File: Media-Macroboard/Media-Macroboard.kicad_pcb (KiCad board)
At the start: 2 copper layers, 100 x 100 mm, 84 parts, among them IC1 MCP73871-4CCI_ML, IC2 LM1117MPX-33NOPB, J1 SS-52400-002, J2 B2B-PH-SM4-TB_LF__SN_, J3 Conn_01x04_MountingPin, Q1 MMBT3904LT3G, Q2 MMBT3904LT3G, Q4 TEMT6000X01, SW1 SW_MEC_5G, SW12 SW_MEC_5G, SW2 SW_MEC_5G, SW3 SW_MEC_5G, SW4 SW_MEC_5G, SW5 SW_MEC_5G, SW6 SW_MEC_5G, SW7 SW_MEC_5G, SW8 SW_MEC_5G, SW9 SW_MEC_5G, U1 ESP32-S3-WROOM-1, U2 USBLC6-2SC6, U3 CP2102N-Axx-xQFN20

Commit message: First productable version
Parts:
- added R23: 470, Resistor_SMD:R_0805_2012Metric_Pad1.20x1.40mm_HandSolder, B.Cu at (100.5, 149.5)
- added R24: 470, Resistor_SMD:R_0805_2012Metric_Pad1.20x1.40mm_HandSolder, B.Cu at (190.0, 151.0)
- added R25: 470, Resistor_SMD:R_0805_2012Metric_Pad1.20x1.40mm_HandSolder, B.Cu at (192.0, 104.0)
- C4, C6, C9: footprint Capacitor_SMD:C_0805_2012Metric_Pad1.18x1.45mm_HandSolder -> Capacitor_SMD:C_1206_3216Metric
- moved U3 13.0 mm to (154.8, 65.0), turned to 90 degrees
- moved LED6 10.8 mm to (155.8, 80.2)
- moved R15 10.8 mm to (155.8, 76.2), turned to -90 degrees
- moved U2 9.95 mm to (164.5, 75.8)
- moved C8 9.55 mm to (176.9, 56.0), turned to 0 degrees
- moved R11 9.00 mm to (159.6, 69.0), turned to 180 degrees
- moved LED2 8.63 mm to (174.9, 77.6)
- moved R9 8.63 mm to (174.9, 81.6)
- moved LED3 8.50 mm to (183.0, 77.5)
- moved R7 8.50 mm to (183.0, 81.4)
- moved Q4 8.36 mm to (168.9, 56.5)
- moved R16 8.02 mm to (159.6, 61.0), turned to 0 degrees
- moved LED5 6.72 mm to (158.2, 80.2)
- moved R14 6.72 mm to (158.2, 76.2), turned to -90 degrees
- moved R12 5.37 mm to (159.6, 67.0), turned to 0 degrees
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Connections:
- LED7 pad 1: Net-(LED10-K) -> Net-(LED7-K)
- LED8 pad 1: Net-(LED10-K) -> Net-(LED8-K)
- LED9 pad 1: Net-(LED10-K) -> Net-(LED9-K)
- R19 pad 1: Net-(LED10-K) -> Net-(LED7-K)
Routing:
- net /ESP32-S3-01/ROW_3: track 0.00 -> 135.2 mm, vias 0 -> 3
- net /ESP32-S3-01/LED3: track 0.00 -> 120.4 mm, vias 0 -> 1
- net /ESP32-S3-01/ROW_2: track 0.00 -> 115.7 mm, vias 0 -> 3
- net /ESP32-S3-01/LED2: track 0.00 -> 107.8 mm, vias 0 -> 1
- net GND: track 0.00 -> 107.2 mm, vias 0 -> 27
- net /ESP32-S3-01/ROW_1: track 0.00 -> 95.9 mm, vias 0 -> 1
- net /ESP32-S3-01/JoyStick_1: track 0.00 -> 95.1 mm, vias 0 -> 2
- net /ESP32-S3-01/JoyStick_Button: track 0.00 -> 92.1 mm, vias 0 -> 2
- net /ESP32-S3-01/JoyStick_2: track 0.00 -> 87.7 mm, vias 0 -> 2
- net /ESP32-S3-01/COL_4: track 0.00 -> 87.0 mm
- net /ESP32-S3-01/COL_1: track 0.00 -> 80.5 mm, vias 0 -> 2
- net /VBUS: track 0.00 -> 77.5 mm, vias 0 -> 2
- net /ESP32-S3-01/LED4: track 0.00 -> 71.1 mm, vias 0 -> 1
- net /ESP32-S3-01/GPIO0: track 0.00 -> 62.4 mm, vias 0 -> 2
- net /ESP32-S3-01/DTR: track 0.00 -> 57.3 mm, vias 0 -> 2
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- added copper zone on F.Cu, net +3.3V

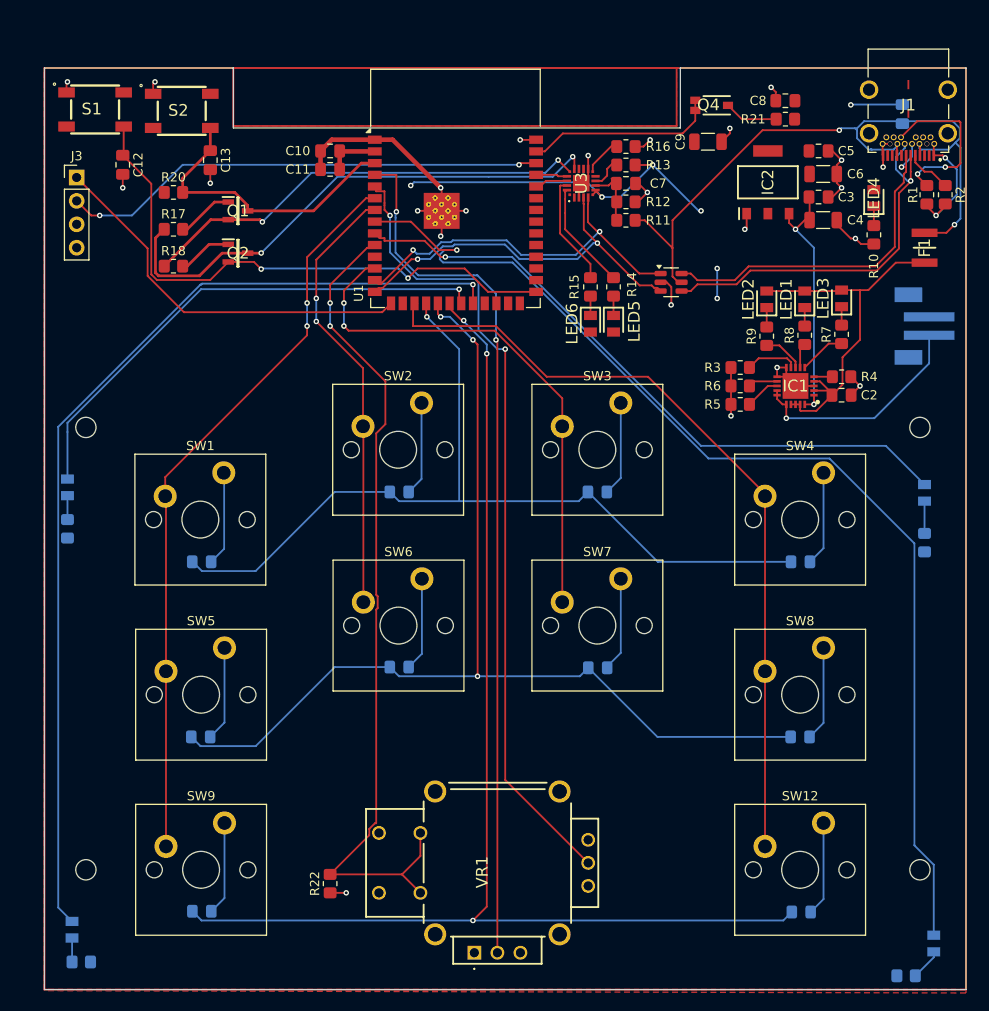
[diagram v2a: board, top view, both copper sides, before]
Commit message: Made four-layer version
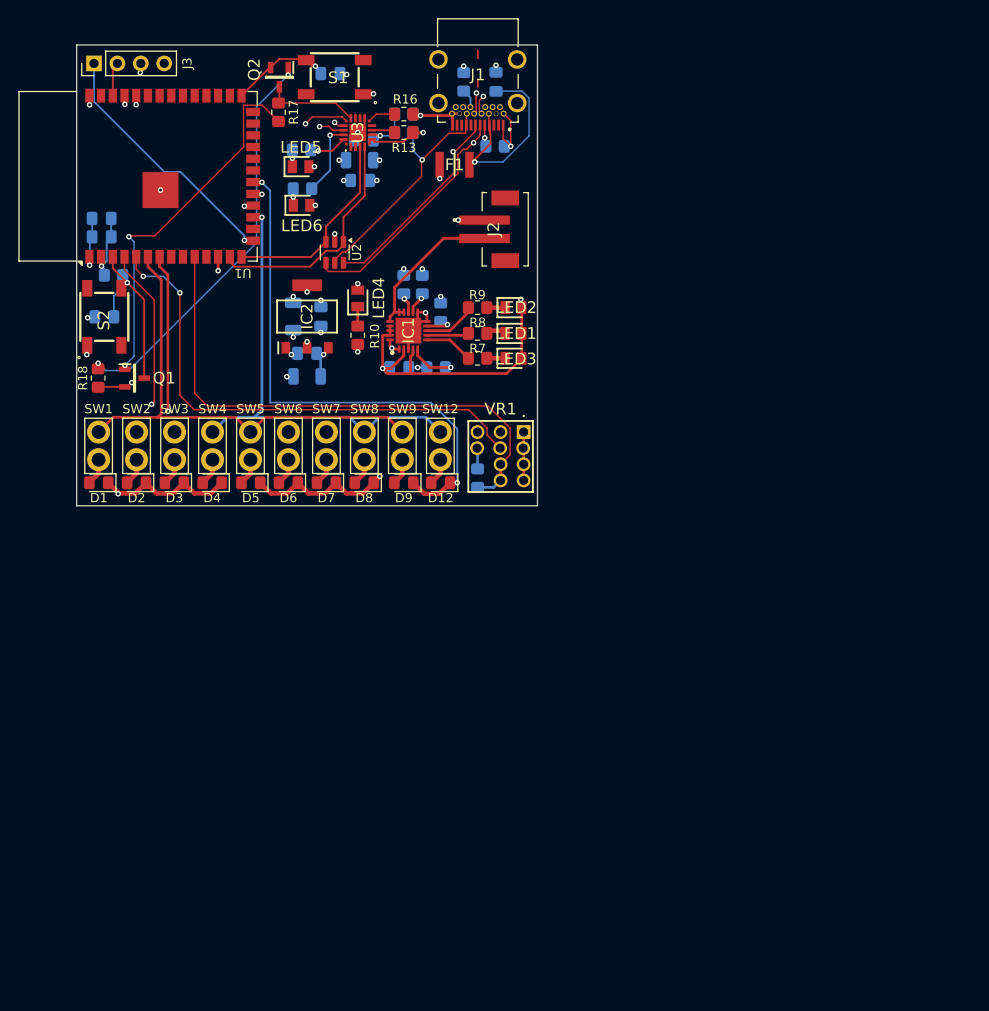
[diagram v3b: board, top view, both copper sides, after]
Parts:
- removed LED10, LED7, LED8, LED9: LTST-C170TBKT, Footprints:LEDC2012X120N
- removed Q4: TEMT6000X01, Footprints:TEMT6000X01
- removed R19, R23, R24, R25: 470, Resistor_SMD:R_0805_2012Metric_Pad1.20x1.40mm_HandSolder
- removed R21: 10K, Resistor_SMD:R_0805_2012Metric_Pad1.20x1.40mm_HandSolder
- removed REF** (x4): MountingHole_2.2mm_M2_ISO14580, MountingHole:MountingHole_2.2mm_M2_ISO14580
- C10, C11, C12, C13, C2, C3, C4, C5, C6, C7, C8, C9, R1, R11, R12, R14, R15, R2, R20, R22, R3, R4, R5, R6: moved to B.Cu
- D1, D12, D2, D3, D4, D5, D6, D7, D8, D9, J2: moved to F.Cu
- SW1, SW12, SW2, SW3, SW4, SW5, SW6, SW7, SW8, SW9: footprint PCM_Switch_Keyboard_Cherry_MX:SW_Cherry_MX_PCB_1.00u -> PCM_Switch_Keyboard_Cherry_MX:SW_Cherry_Compact
- moved D4 64.4 mm to (114.7, 97.5), turned to 180 degrees
- moved SW4 64.3 mm to (114.7, 93.5)
- moved D12 60.8 mm to (139.5, 97.5), turned to 180 degrees
- moved SW12 60.3 mm to (139.5, 93.5)
- moved C6 59.5 mm to (123.5, 79.5), turned to -90 degrees
- moved C4 58.5 mm to (125.0, 86.0), turned to 180 degrees
- moved C3 58.0 mm to (125.0, 83.5), turned to 180 degrees
- moved LED4 57.1 mm to (130.5, 77.5)
- moved R10 57.1 mm to (130.5, 81.5)
- moved C5 56.9 mm to (126.5, 79.5), turned to -90 degrees
- moved VR1 56.8 mm to (148.5, 92.0), turned to -90 degrees
- moved D8 54.8 mm to (131.2, 97.5), turned to 180 degrees
- moved SW8 54.4 mm to (131.2, 93.5)
- moved IC2 52.1 mm to (125.0, 79.5)
- moved F1 51.8 mm to (141.0, 63.0), turned to 0 degrees
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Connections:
- U1 pad 21: /ESP32-S3-01/LED1 -> unconnected-(U1-IO13-Pad21)
- U1 pad 22: /ESP32-S3-01/LED2 -> unconnected-(U1-IO14-Pad22)
- U1 pad 39: /ESP32-S3-01/Light -> unconnected-(U1-IO1-Pad39)
- U1 pad 8: /ESP32-S3-01/LED3 -> unconnected-(U1-IO15-Pad8)
- U1 pad 9: /ESP32-S3-01/LED4 -> unconnected-(U1-IO16-Pad9)
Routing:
- net /ESP32-S3-01/LED3: track 120.4 -> 0.00 mm, vias 1 -> 0
- net /ESP32-S3-01/LED2: track 107.8 -> 0.00 mm, vias 1 -> 0
- net /ESP32-S3-01/ROW_3: track 135.2 -> 56.6 mm, vias 3 -> 2
- net GND: track 107.2 -> 33.1 mm, vias 27 -> 26
- net /ESP32-S3-01/LED4: track 71.1 -> 0.00 mm, vias 1 -> 0
- net /ESP32-S3-01/ROW_2: track 115.7 -> 57.8 mm, vias 3 -> 2
- net /ESP32-S3-01/LED1: track 56.2 -> 0.00 mm, vias 1 -> 0
- net /ESP32-S3-01/GPIO0: track 62.4 -> 9.98 mm, vias 2 -> 1
- net /ESP32-S3-01/SCL: track 52.9 -> 3.71 mm, vias 2 -> 0
- net /ESP32-S3-01/DTR: track 57.3 -> 10.3 mm, vias 2 -> 0
- net /ESP32-S3-01/ROW_1: track 95.9 -> 52.2 mm, vias 1 -> 2
- net /ESP32-S3-01/JoyStick_1: track 95.1 -> 56.5 mm, vias 2 -> 1
- net /ESP32-S3-01/COL_4: track 87.0 -> 49.4 mm, vias 0 -> 1
- net Net-(Q2-B): track 5.93 -> 42.9 mm, vias 0 -> 2
- net Net-(Q1-B): track 6.17 -> 40.1 mm, vias 0 -> 2
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- added copper zone on In1.Cu, net +3.3V
- added copper zone on In2.Cu, net GND
- removed copper zone on F.Cu, net +3.3V
- removed copper zone on B.Cu, net GND
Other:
- board size 100 x 100 mm -> 50 x 50 mm
- copper layers 2 -> 4

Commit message: Added more rows and columns
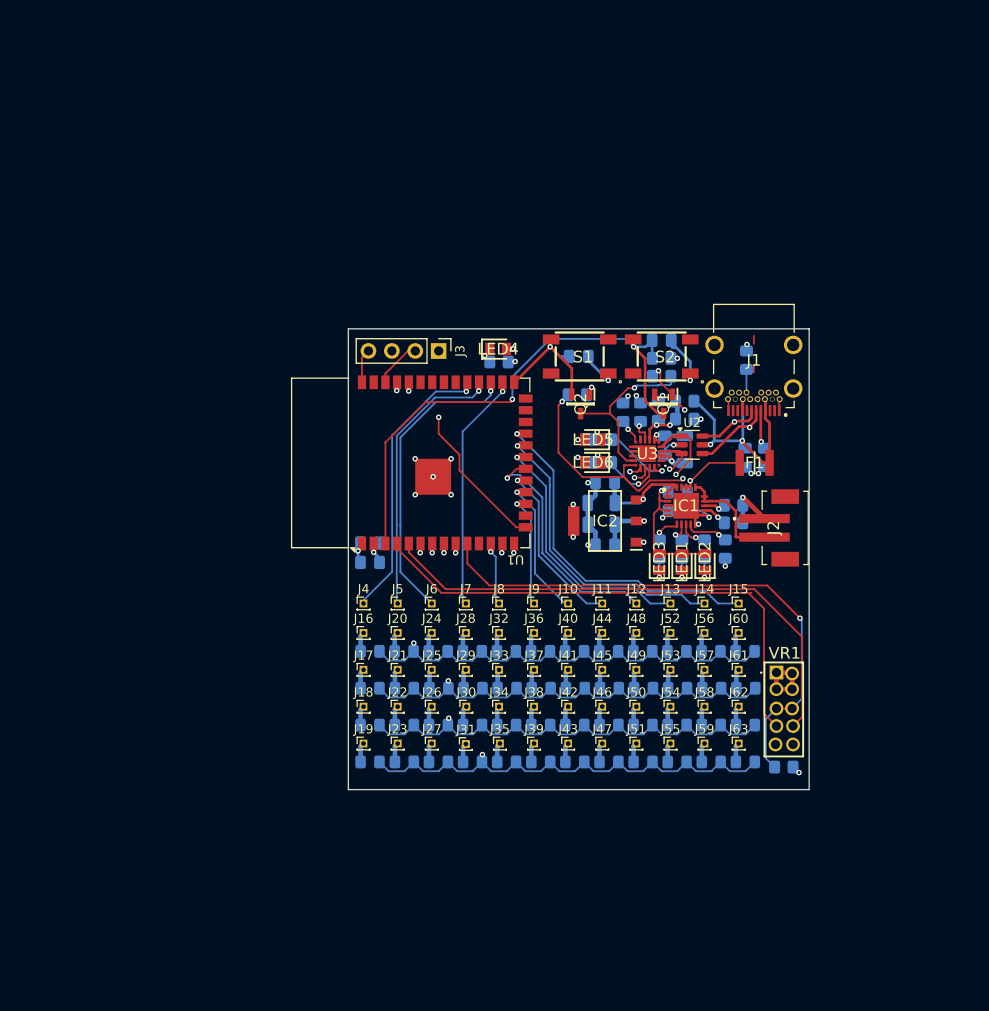
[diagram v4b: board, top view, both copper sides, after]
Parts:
- removed SW1, SW12, SW2, SW3, SW4, SW5, SW6, SW7, SW8, SW9: SW_MEC_5G, PCM_Switch_Keyboard_Cherry_MX:SW_Cherry_Compact
- added D10: D, Diode_SMD:D_0805_2012Metric_Pad1.15x1.40mm_HandSolder, B.Cu at (135.6, 123.8)
- added D11: D, Diode_SMD:D_0805_2012Metric_Pad1.15x1.40mm_HandSolder, B.Cu at (139.3, 123.8)
- added D13: D, Diode_SMD:D_0805_2012Metric_Pad1.15x1.40mm_HandSolder, B.Cu at (131.8, 127.8)
- added D14: D, Diode_SMD:D_0805_2012Metric_Pad1.15x1.40mm_HandSolder, B.Cu at (135.6, 127.8)
- added D15: D, Diode_SMD:D_0805_2012Metric_Pad1.15x1.40mm_HandSolder, B.Cu at (139.3, 127.8)
- added D16: D, Diode_SMD:D_0805_2012Metric_Pad1.15x1.40mm_HandSolder, B.Cu at (143.0, 127.8)
- added D17: D, Diode_SMD:D_0805_2012Metric_Pad1.15x1.40mm_HandSolder, B.Cu at (146.6, 115.8)
- added D18: D, Diode_SMD:D_0805_2012Metric_Pad1.15x1.40mm_HandSolder, B.Cu at (146.7, 119.8)
- added D19: D, Diode_SMD:D_0805_2012Metric_Pad1.15x1.40mm_HandSolder, B.Cu at (146.7, 123.8)
- added D20: D, Diode_SMD:D_0805_2012Metric_Pad1.15x1.40mm_HandSolder, B.Cu at (146.7, 127.8)
- added D21: D, Diode_SMD:D_0805_2012Metric_Pad1.15x1.40mm_HandSolder, B.Cu at (150.3, 115.8)
- added D22: D, Diode_SMD:D_0805_2012Metric_Pad1.15x1.40mm_HandSolder, B.Cu at (150.4, 119.8)
- added D23: D, Diode_SMD:D_0805_2012Metric_Pad1.15x1.40mm_HandSolder, B.Cu at (150.4, 123.8)
- added D24: D, Diode_SMD:D_0805_2012Metric_Pad1.15x1.40mm_HandSolder, B.Cu at (150.4, 127.8)
- added D25: D, Diode_SMD:D_0805_2012Metric_Pad1.15x1.40mm_HandSolder, B.Cu at (154.0, 115.8)
- added D26: D, Diode_SMD:D_0805_2012Metric_Pad1.15x1.40mm_HandSolder, B.Cu at (154.1, 119.8)
- added D27: D, Diode_SMD:D_0805_2012Metric_Pad1.15x1.40mm_HandSolder, B.Cu at (154.1, 123.8)
- added D28: D, Diode_SMD:D_0805_2012Metric_Pad1.15x1.40mm_HandSolder, B.Cu at (154.1, 127.8)
- added D29: D, Diode_SMD:D_0805_2012Metric_Pad1.15x1.40mm_HandSolder, B.Cu at (157.7, 115.8)
- added D30: D, Diode_SMD:D_0805_2012Metric_Pad1.15x1.40mm_HandSolder, B.Cu at (157.8, 119.8)
- added D31: D, Diode_SMD:D_0805_2012Metric_Pad1.15x1.40mm_HandSolder, B.Cu at (157.8, 123.8)
- added D32: D, Diode_SMD:D_0805_2012Metric_Pad1.15x1.40mm_HandSolder, B.Cu at (157.8, 127.8)
- added D33: D, Diode_SMD:D_0805_2012Metric_Pad1.15x1.40mm_HandSolder, B.Cu at (161.4, 115.8)
- added D34: D, Diode_SMD:D_0805_2012Metric_Pad1.15x1.40mm_HandSolder, B.Cu at (161.5, 119.8)
- added D35: D, Diode_SMD:D_0805_2012Metric_Pad1.15x1.40mm_HandSolder, B.Cu at (161.5, 123.8)
- added D36: D, Diode_SMD:D_0805_2012Metric_Pad1.15x1.40mm_HandSolder, B.Cu at (161.5, 127.8)
- added D37: D, Diode_SMD:D_0805_2012Metric_Pad1.15x1.40mm_HandSolder, B.Cu at (165.1, 115.8)
- added D38: D, Diode_SMD:D_0805_2012Metric_Pad1.15x1.40mm_HandSolder, B.Cu at (165.2, 119.8)
- added D39: D, Diode_SMD:D_0805_2012Metric_Pad1.15x1.40mm_HandSolder, B.Cu at (165.2, 123.8)
- added D40: D, Diode_SMD:D_0805_2012Metric_Pad1.15x1.40mm_HandSolder, B.Cu at (165.2, 127.8)
- added D41: D, Diode_SMD:D_0805_2012Metric_Pad1.15x1.40mm_HandSolder, B.Cu at (168.8, 115.8)
- added D42: D, Diode_SMD:D_0805_2012Metric_Pad1.15x1.40mm_HandSolder, B.Cu at (168.9, 119.8)
- added D43: D, Diode_SMD:D_0805_2012Metric_Pad1.15x1.40mm_HandSolder, B.Cu at (168.9, 123.8)
- added D44: D, Diode_SMD:D_0805_2012Metric_Pad1.15x1.40mm_HandSolder, B.Cu at (168.9, 127.8)
- added D45: D, Diode_SMD:D_0805_2012Metric_Pad1.15x1.40mm_HandSolder, B.Cu at (172.5, 115.8)
- added D46: D, Diode_SMD:D_0805_2012Metric_Pad1.15x1.40mm_HandSolder, B.Cu at (172.6, 119.8)
- added D47: D, Diode_SMD:D_0805_2012Metric_Pad1.15x1.40mm_HandSolder, B.Cu at (172.6, 123.8)
- added D48: D, Diode_SMD:D_0805_2012Metric_Pad1.15x1.40mm_HandSolder, B.Cu at (172.6, 127.8)
- added J10: Conn_01x01_Pin, Connector_PinHeader_1.00mm:PinHeader_1x01_P1.00mm_Vertical, F.Cu at (153.3, 110.6)
- added J11: Conn_01x01_Pin, Connector_PinHeader_1.00mm:PinHeader_1x01_P1.00mm_Vertical, F.Cu at (157.0, 110.6)
- added J12: Conn_01x01_Pin, Connector_PinHeader_1.00mm:PinHeader_1x01_P1.00mm_Vertical, F.Cu at (160.7, 110.6)
- added J13: Conn_01x01_Pin, Connector_PinHeader_1.00mm:PinHeader_1x01_P1.00mm_Vertical, F.Cu at (164.4, 110.6)
- added J14: Conn_01x01_Pin, Connector_PinHeader_1.00mm:PinHeader_1x01_P1.00mm_Vertical, F.Cu at (168.1, 110.6)
- added J15: Conn_01x01_Pin, Connector_PinHeader_1.00mm:PinHeader_1x01_P1.00mm_Vertical, F.Cu at (171.8, 110.6)
- added J16: Conn_01x01_Pin, Connector_PinHeader_1.00mm:PinHeader_1x01_P1.00mm_Vertical, F.Cu at (131.1, 113.8)
- added J17: Conn_01x01_Pin, Connector_PinHeader_1.00mm:PinHeader_1x01_P1.00mm_Vertical, F.Cu at (131.1, 117.8)
- added J18: Conn_01x01_Pin, Connector_PinHeader_1.00mm:PinHeader_1x01_P1.00mm_Vertical, F.Cu at (131.1, 121.8)
- added J19: Conn_01x01_Pin, Connector_PinHeader_1.00mm:PinHeader_1x01_P1.00mm_Vertical, F.Cu at (131.1, 125.8)
- added J20: Conn_01x01_Pin, Connector_PinHeader_1.00mm:PinHeader_1x01_P1.00mm_Vertical, F.Cu at (134.8, 113.8)
- added J21: Conn_01x01_Pin, Connector_PinHeader_1.00mm:PinHeader_1x01_P1.00mm_Vertical, F.Cu at (134.8, 117.8)
- added J22: Conn_01x01_Pin, Connector_PinHeader_1.00mm:PinHeader_1x01_P1.00mm_Vertical, F.Cu at (134.8, 121.8)
- added J23: Conn_01x01_Pin, Connector_PinHeader_1.00mm:PinHeader_1x01_P1.00mm_Vertical, F.Cu at (134.8, 125.8)
- added J24: Conn_01x01_Pin, Connector_PinHeader_1.00mm:PinHeader_1x01_P1.00mm_Vertical, F.Cu at (138.5, 113.8)
- added J25: Conn_01x01_Pin, Connector_PinHeader_1.00mm:PinHeader_1x01_P1.00mm_Vertical, F.Cu at (138.5, 117.8)
- added J26: Conn_01x01_Pin, Connector_PinHeader_1.00mm:PinHeader_1x01_P1.00mm_Vertical, F.Cu at (138.5, 121.8)
- added J27: Conn_01x01_Pin, Connector_PinHeader_1.00mm:PinHeader_1x01_P1.00mm_Vertical, F.Cu at (138.5, 125.8)
- added J28: Conn_01x01_Pin, Connector_PinHeader_1.00mm:PinHeader_1x01_P1.00mm_Vertical, F.Cu at (142.2, 113.8)
- added J29: Conn_01x01_Pin, Connector_PinHeader_1.00mm:PinHeader_1x01_P1.00mm_Vertical, F.Cu at (142.2, 117.8)
- added J30: Conn_01x01_Pin, Connector_PinHeader_1.00mm:PinHeader_1x01_P1.00mm_Vertical, F.Cu at (142.3, 121.8)
- added J31: Conn_01x01_Pin, Connector_PinHeader_1.00mm:PinHeader_1x01_P1.00mm_Vertical, F.Cu at (142.2, 125.8)
- added J32: Conn_01x01_Pin, Connector_PinHeader_1.00mm:PinHeader_1x01_P1.00mm_Vertical, F.Cu at (145.8, 113.8)
- added J33: Conn_01x01_Pin, Connector_PinHeader_1.00mm:PinHeader_1x01_P1.00mm_Vertical, F.Cu at (145.8, 117.8)
- added J34: Conn_01x01_Pin, Connector_PinHeader_1.00mm:PinHeader_1x01_P1.00mm_Vertical, F.Cu at (145.8, 121.8)
- added J35: Conn_01x01_Pin, Connector_PinHeader_1.00mm:PinHeader_1x01_P1.00mm_Vertical, F.Cu at (145.9, 125.8)
- added J36: Conn_01x01_Pin, Connector_PinHeader_1.00mm:PinHeader_1x01_P1.00mm_Vertical, F.Cu at (149.6, 113.8)
- added J37: Conn_01x01_Pin, Connector_PinHeader_1.00mm:PinHeader_1x01_P1.00mm_Vertical, F.Cu at (149.6, 117.8)
- added J38: Conn_01x01_Pin, Connector_PinHeader_1.00mm:PinHeader_1x01_P1.00mm_Vertical, F.Cu at (149.6, 121.8)
- added J39: Conn_01x01_Pin, Connector_PinHeader_1.00mm:PinHeader_1x01_P1.00mm_Vertical, F.Cu at (149.6, 125.8)
- added J4: Conn_01x01_Pin, Connector_PinHeader_1.00mm:PinHeader_1x01_P1.00mm_Vertical, F.Cu at (131.1, 110.6)
- added J40: Conn_01x01_Pin, Connector_PinHeader_1.00mm:PinHeader_1x01_P1.00mm_Vertical, F.Cu at (153.3, 113.8)
- added J41: Conn_01x01_Pin, Connector_PinHeader_1.00mm:PinHeader_1x01_P1.00mm_Vertical, F.Cu at (153.3, 117.8)
- added J42: Conn_01x01_Pin, Connector_PinHeader_1.00mm:PinHeader_1x01_P1.00mm_Vertical, F.Cu at (153.3, 121.8)
- added J43: Conn_01x01_Pin, Connector_PinHeader_1.00mm:PinHeader_1x01_P1.00mm_Vertical, F.Cu at (153.3, 125.8)
- added J44: Conn_01x01_Pin, Connector_PinHeader_1.00mm:PinHeader_1x01_P1.00mm_Vertical, F.Cu at (157.0, 113.8)
- added J45: Conn_01x01_Pin, Connector_PinHeader_1.00mm:PinHeader_1x01_P1.00mm_Vertical, F.Cu at (157.0, 117.8)
- added J46: Conn_01x01_Pin, Connector_PinHeader_1.00mm:PinHeader_1x01_P1.00mm_Vertical, F.Cu at (157.0, 121.8)
- added J47: Conn_01x01_Pin, Connector_PinHeader_1.00mm:PinHeader_1x01_P1.00mm_Vertical, F.Cu at (157.0, 125.8)
- added J48: Conn_01x01_Pin, Connector_PinHeader_1.00mm:PinHeader_1x01_P1.00mm_Vertical, F.Cu at (160.7, 113.8)
- added J49: Conn_01x01_Pin, Connector_PinHeader_1.00mm:PinHeader_1x01_P1.00mm_Vertical, F.Cu at (160.7, 117.8)
- added J5: Conn_01x01_Pin, Connector_PinHeader_1.00mm:PinHeader_1x01_P1.00mm_Vertical, F.Cu at (134.8, 110.6)
- added J50: Conn_01x01_Pin, Connector_PinHeader_1.00mm:PinHeader_1x01_P1.00mm_Vertical, F.Cu at (160.7, 121.8)
- added J51: Conn_01x01_Pin, Connector_PinHeader_1.00mm:PinHeader_1x01_P1.00mm_Vertical, F.Cu at (160.7, 125.8)
- added J52: Conn_01x01_Pin, Connector_PinHeader_1.00mm:PinHeader_1x01_P1.00mm_Vertical, F.Cu at (164.4, 113.8)
- added J53: Conn_01x01_Pin, Connector_PinHeader_1.00mm:PinHeader_1x01_P1.00mm_Vertical, F.Cu at (164.4, 117.8)
- added J54: Conn_01x01_Pin, Connector_PinHeader_1.00mm:PinHeader_1x01_P1.00mm_Vertical, F.Cu at (164.4, 121.8)
- added J55: Conn_01x01_Pin, Connector_PinHeader_1.00mm:PinHeader_1x01_P1.00mm_Vertical, F.Cu at (164.4, 125.8)
- added J56: Conn_01x01_Pin, Connector_PinHeader_1.00mm:PinHeader_1x01_P1.00mm_Vertical, F.Cu at (168.1, 113.8)
- added J57: Conn_01x01_Pin, Connector_PinHeader_1.00mm:PinHeader_1x01_P1.00mm_Vertical, F.Cu at (168.1, 117.8)
- added J58: Conn_01x01_Pin, Connector_PinHeader_1.00mm:PinHeader_1x01_P1.00mm_Vertical, F.Cu at (168.1, 121.8)
- added J59: Conn_01x01_Pin, Connector_PinHeader_1.00mm:PinHeader_1x01_P1.00mm_Vertical, F.Cu at (168.1, 125.8)
- added J6: Conn_01x01_Pin, Connector_PinHeader_1.00mm:PinHeader_1x01_P1.00mm_Vertical, F.Cu at (138.5, 110.6)
- added J60: Conn_01x01_Pin, Connector_PinHeader_1.00mm:PinHeader_1x01_P1.00mm_Vertical, F.Cu at (171.8, 113.8)
- added J61: Conn_01x01_Pin, Connector_PinHeader_1.00mm:PinHeader_1x01_P1.00mm_Vertical, F.Cu at (171.8, 117.8)
- added J62: Conn_01x01_Pin, Connector_PinHeader_1.00mm:PinHeader_1x01_P1.00mm_Vertical, F.Cu at (171.8, 121.8)
- added J63: Conn_01x01_Pin, Connector_PinHeader_1.00mm:PinHeader_1x01_P1.00mm_Vertical, F.Cu at (171.8, 125.8)
- added J7: Conn_01x01_Pin, Connector_PinHeader_1.00mm:PinHeader_1x01_P1.00mm_Vertical, F.Cu at (142.2, 110.6)
- added J8: Conn_01x01_Pin, Connector_PinHeader_1.00mm:PinHeader_1x01_P1.00mm_Vertical, F.Cu at (145.8, 110.6)
- added J9: Conn_01x01_Pin, Connector_PinHeader_1.00mm:PinHeader_1x01_P1.00mm_Vertical, F.Cu at (149.6, 110.6)
- D1, D12, D2, D3, D4, D5, D6, D7, D8, D9, R10, R13, R16, R17, R18, R7, R8, R9: moved to B.Cu
- moved S2 60.6 mm to (163.5, 83.8), turned to 180 degrees
- moved C13 60.5 mm to (163.5, 82.0), turned to 0 degrees
- moved R20 60.2 mm to (163.5, 84.0), turned to 180 degrees
- moved Q1 57.5 mm to (163.7, 89.0), turned to -90 degrees
- moved R18 52.0 mm to (154.3, 88.0), turned to 0 degrees
- moved R17 50.5 mm to (163.5, 86.0), turned to 180 degrees
- moved C1 48.9 mm to (172.5, 94.8), turned to -90 degrees
- moved J3 48.7 mm to (139.3, 83.2), turned to -90 degrees
- moved Q2 48.2 mm to (154.7, 89.0)
- moved C11 47.3 mm to (131.8, 106.2)
- moved C9 47.2 mm to (166.0, 93.9), turned to -90 degrees
- moved U3 46.9 mm to (161.9, 94.3), turned to 180 degrees
- moved F1 45.9 mm to (173.6, 95.3)
- moved R22 45.7 mm to (176.7, 128.3), turned to 180 degrees
- moved R14 45.3 mm to (157.1, 92.8)
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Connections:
- U1 pad 12: /ESP32-S3-01/COL_3 -> /ESP32-S3-01/COL_5
- U1 pad 17: /ESP32-S3-01/COL_4 -> /ESP32-S3-01/COL_6
- U1 pad 18: /ESP32-S3-01/ROW_1 -> /ESP32-S3-01/COL_7
- U1 pad 19: /ESP32-S3-01/ROW_2 -> /ESP32-S3-01/COL_8
- U1 pad 20: /ESP32-S3-01/ROW_3 -> /ESP32-S3-01/COL_9
- U1 pad 21: unconnected-(U1-IO13-Pad21) -> /ESP32-S3-01/COL_10
- U1 pad 22: unconnected-(U1-IO14-Pad22) -> /ESP32-S3-01/COL_11
- U1 pad 23: unconnected-(U1-IO21-Pad23) -> /ESP32-S3-01/COL_12
- U1 pad 28: unconnected-(U1-IO35-Pad28) -> /ESP32-S3-01/COL_4
- U1 pad 29: unconnected-(U1-IO36-Pad29) -> /ESP32-S3-01/COL_3
- U1 pad 30: unconnected-(U1-IO37-Pad30) -> /ESP32-S3-01/COL_2
- U1 pad 31: unconnected-(U1-IO38-Pad31) -> /ESP32-S3-01/COL_1
- U1 pad 6: /ESP32-S3-01/COL_1 -> /ESP32-S3-01/ROW_1
- U1 pad 7: /ESP32-S3-01/COL_2 -> /ESP32-S3-01/ROW_2
- U1 pad 8: unconnected-(U1-IO15-Pad8) -> /ESP32-S3-01/ROW_3
- U1 pad 9: unconnected-(U1-IO16-Pad9) -> /ESP32-S3-01/ROW_4
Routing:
- net /ESP32-S3-01/ROW_4: track 0.00 -> 73.0 mm, vias 0 -> 2
- net Net-(Q2-B): track 42.9 -> 0.00 mm, vias 2 -> 1
- net /ESP32-S3-01/CHIP_PU: track 18.9 -> 57.8 mm, vias 1 -> 2
- net Net-(Q1-B): track 40.1 -> 3.17 mm, vias 2 -> 1
- net /ESP32-S3-01/COL_12: track 0.00 -> 36.7 mm, vias 0 -> 1
- net /ESP32-S3-01/COL_11: track 0.00 -> 32.0 mm, vias 0 -> 1
- net /VBUS: track 53.8 -> 25.7 mm
- net /ESP32-S3-01/COL_10: track 0.00 -> 27.4 mm, vias 0 -> 1
- net /ESP32-S3-01/COL_9: track 0.00 -> 25.9 mm, vias 0 -> 1
- net /+5V_USB: track 51.3 -> 26.0 mm, vias 3 -> 2
- net /ESP32-S3-01/COL_4: track 49.4 -> 24.8 mm
- net /ESP32-S3-01/COL_1: track 53.8 -> 29.7 mm, vias 0 -> 1
- net +3.3V: track 45.0 -> 66.7 mm, vias 12 -> 10
- net /USB_DP: track 31.5 -> 11.4 mm, vias 2 -> 1
- net GND: track 33.1 -> 52.3 mm, vias 26 -> 25
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- added copper zone on In2.Cu, net +3.3V
- added copper zone on In1.Cu, net GND
- removed copper zone on In1.Cu, net +3.3V
- removed copper zone on In2.Cu, net GND
